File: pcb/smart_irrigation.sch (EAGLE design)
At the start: 13 parts, among them IC1 7805DT, IC2 7833DT, J1 1X2-3.5MM

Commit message: Add BL600 with autorun jumper to PCB
The autorun jumper is used to enable and disable the autorun feature of
the BL600.
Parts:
- added JP1: (no value), pinhead:PINHD-1X6
- added U$1: BL600, library:BL600
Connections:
- removed net +3.3V: C10.1, C3.1, IC2.VO
- new net +3V3: C10.1, C3.1, IC2.VO, JP1.3, JP1.6, U$1.VCC@1, U$1.VCC@2
- new net N$2: JP1.2, U$1.!AUTORUN
- new net N$5: JP1.5, U$1.SIO7
- net GND: now also JP1.1, JP1.4, U$1.GND@1, U$1.GND@2, U$1.GND@3, U$1.GND@4, U$1.GND@5
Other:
- note added: "AUTORUN JUMPER"
- note added: "Enable: Jump 1, 2 Disable: Jump 2, 3"
- moved on the sheet: C1, C10, C2, C3, C4, C5, C6, C7, C8, C9, IC1, IC2

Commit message: Rename EAGLE library file
Schematic and board files updated to use new library filename
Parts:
- IC2: device library:7833DT -> smart_irrigation:7833DT
- U$1: device library:BL600 -> smart_irrigation:BL600
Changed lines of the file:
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@@
 <setting verticaltext="up"/>
 </settings>
-<grid distance="0.1" unitdist="inch" unit="inch" style="lines" multiple="1" display="yes" altdistance="0.01" altunitdist="inch" altunit="inch"/>
+<grid distance="0.1" unitdist="inch" unit="inch" style="lines" multiple="1" display="no" altdistance="0.01" altunitdist="inch" altunit="inch"/>
 <layers>
 <layer number="1" name="Top" color="4" fill="1" visible="no" active="no"/>
@@
 <part name="SUPPLY9" library="supply2" deviceset="GND" device=""/>
 <part name="SUPPLY10" library="supply2" deviceset="GND" device=""/>
-<part name="IC2" library="library" deviceset="78" device="DT" technology="33"/>
+<part name="IC2" library="smart_irrigation" deviceset="78" device="DT" technology="33"/>
 <part name="SUPPLY4" library="supply2" deviceset="GND" device=""/>
 <part name="SUPPLY5" library="supply2" deviceset="GND" device=""/>
@@
 <part name="SUPPLY15" library="supply2" deviceset="+9V" device=""/>
 <part name="SUPPLY16" library="supply2" deviceset="+9V" device=""/>
-<part name="U$1" library="library" deviceset="BL600" device=""/>
+<part name="U$1" library="smart_irrigation" deviceset="BL600" device=""/>
 <part name="FRAME1" library="frames" deviceset="FRAME_A_L" device=""/>
 <part name="SUPPLY17" library="supply2" deviceset="GND" device=""/>

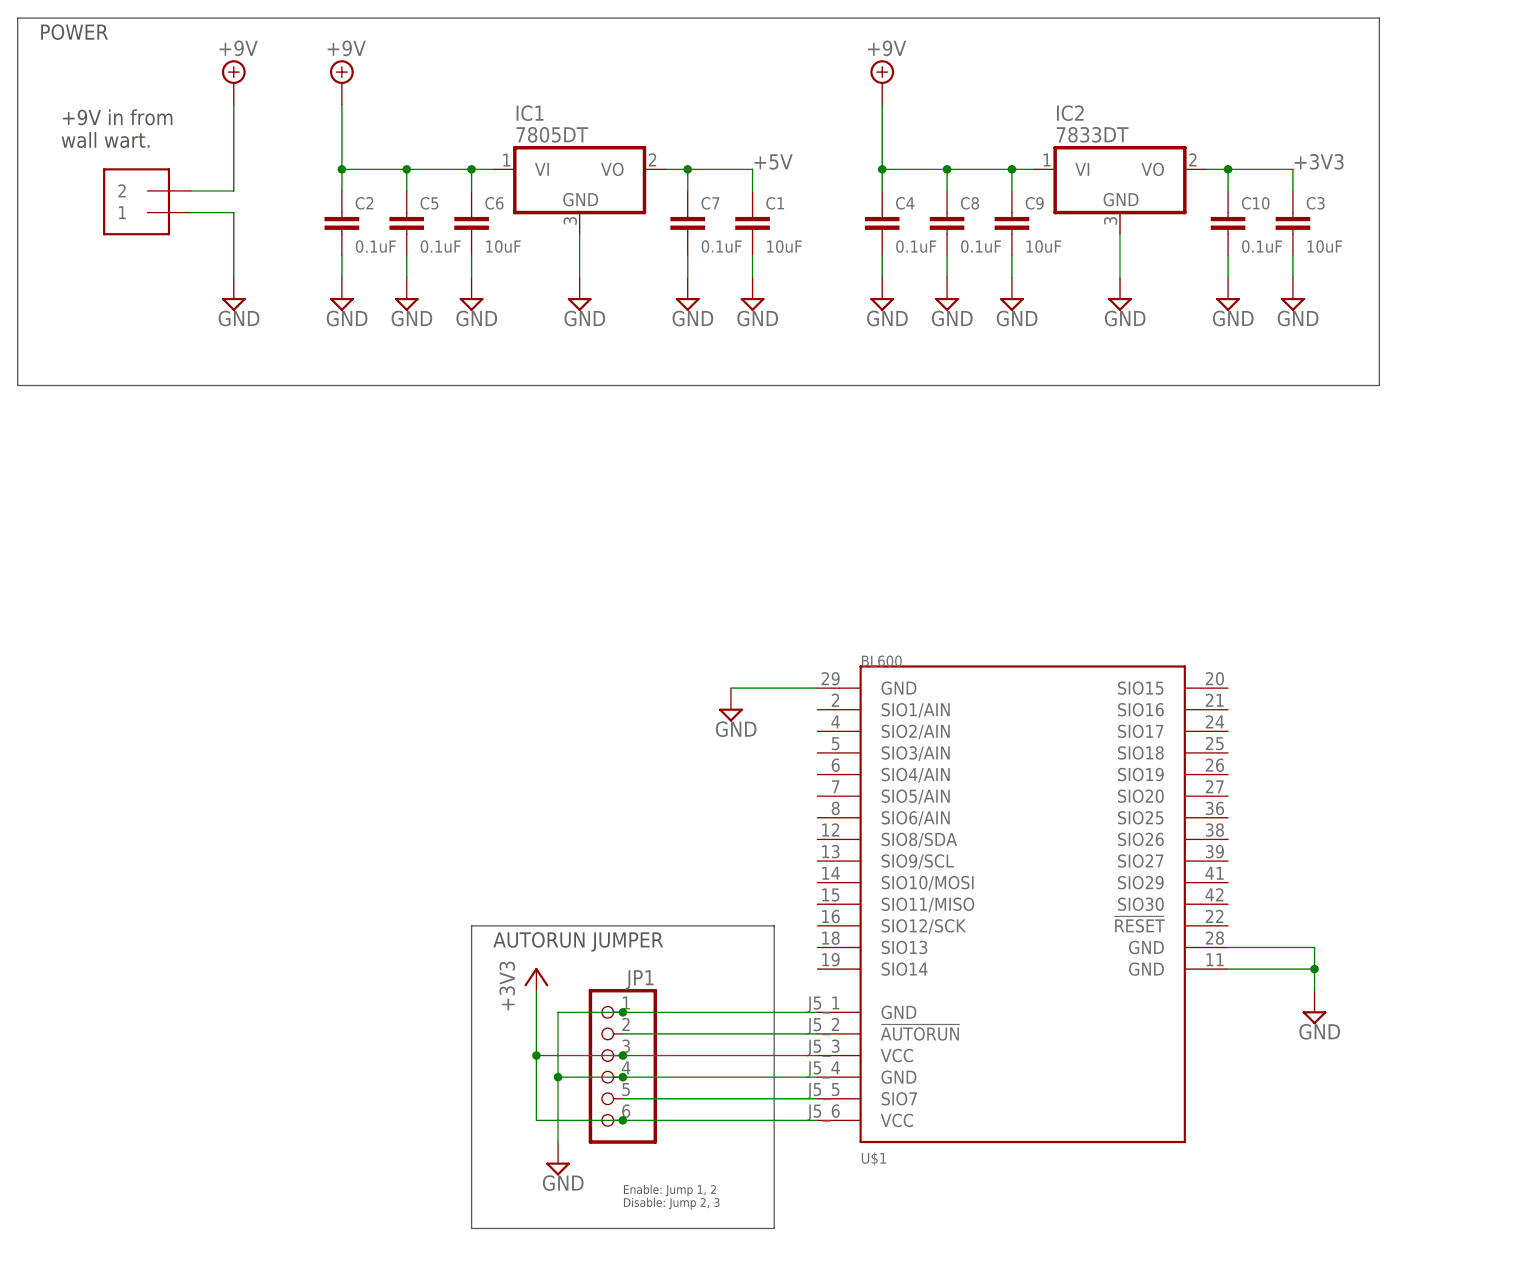
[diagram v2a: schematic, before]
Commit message: PCB: Add external headers
Having the breakout board pins run to external headers allows for both
debugging and adding additional peripherals if needed.
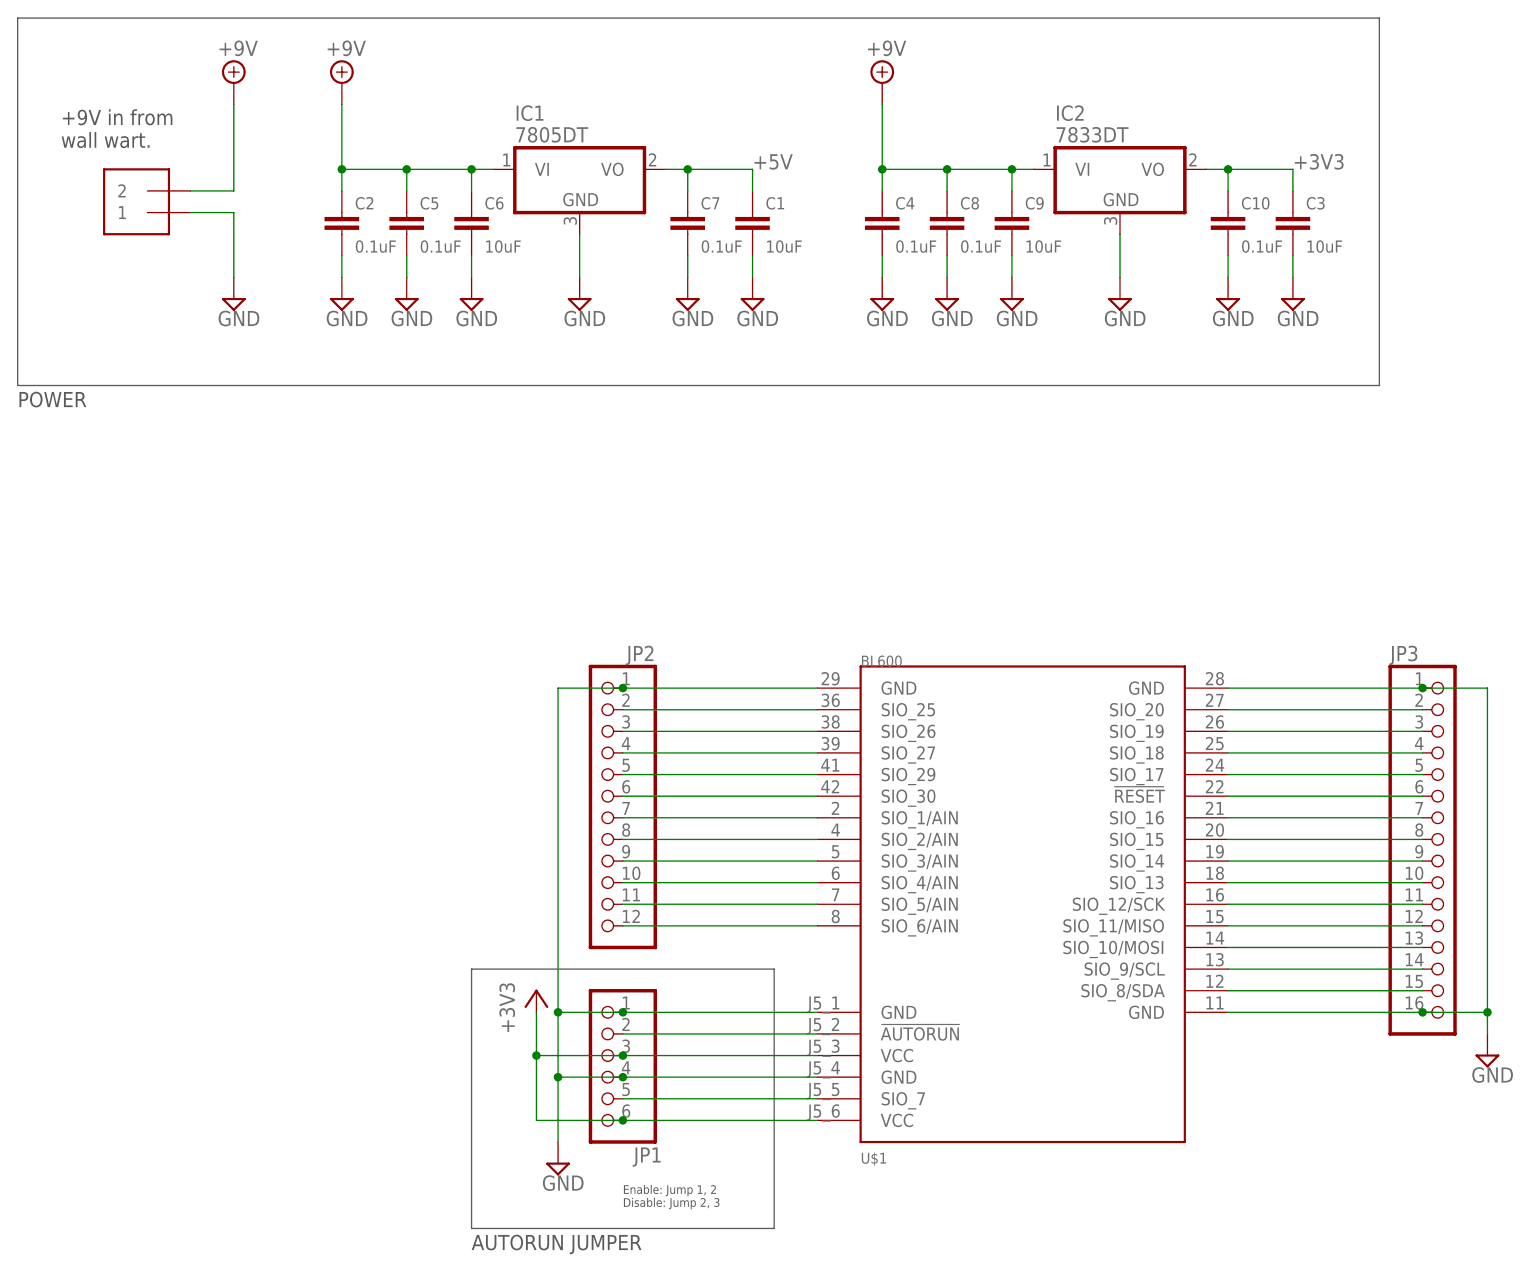
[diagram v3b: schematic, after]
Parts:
- added JP2: (no value), pinhead:PINHD-1X12
- added JP3: (no value), pinhead:PINHD-1X16
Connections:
- new net N$10: JP2.8, U$1.SIO_2/AIN
- new net N$11: JP2.9, U$1.SIO_3/AIN
- new net N$12: JP2.10, U$1.SIO_4/AIN
- new net N$13: JP2.11, U$1.SIO_5/AIN
- new net N$14: JP2.12, U$1.SIO_6/AIN
- new net N$16: JP3.2, U$1.SIO_20
- new net N$17: JP3.3, U$1.SIO_19
- new net N$18: JP3.4, U$1.SIO_18
- new net N$19: JP3.5, U$1.SIO_17
- new net N$2: JP1.5, U$1.SIO_7
- new net N$20: JP3.6, U$1.!RESET
- new net N$21: JP3.7, U$1.SIO_16
- new net N$22: JP3.8, U$1.SIO_15
- new net N$23: JP3.9, U$1.SIO_14
- new net N$24: JP3.10, U$1.SIO_13
- new net N$25: JP3.11, U$1.SIO_12/SCK
- new net N$26: JP3.12, U$1.SIO_11/MISO
- new net N$27: JP3.13, U$1.SIO_10/MOSI
- new net N$28: JP3.14, U$1.SIO_9/SCL
- new net N$29: JP3.15, U$1.SIO_8/SDA
- new net N$4: JP2.2, U$1.SIO_25
- new net N$6: JP2.4, U$1.SIO_27
- new net N$7: JP2.5, U$1.SIO_29
- new net N$8: JP2.6, U$1.SIO_30
- new net N$9: JP2.7, U$1.SIO_1/AIN
- net GND: now also JP2.1, JP3.1, JP3.16
- net N$5: now also JP2.3, U$1.SIO_26; no longer JP1.5, U$1.SIO7
